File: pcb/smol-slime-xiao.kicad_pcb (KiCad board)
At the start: 4 copper layers, 20 x 23.5 mm, 12 parts, among them J1 Conn_01x02, J2 Conn_01x02, U1 ICM-45686, U3 1532H, U4 XIAO-nRF52840-SMD

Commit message: Add pours
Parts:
- moved C3 0.72 mm to (153.8, 108.3)
- moved R1 0.70 mm to (145.2, 107.3)
- moved R2 0.70 mm to (145.2, 109.0)
- moved U3 0.64 mm to (156.4, 92.5)
- moved R3 0.53 mm to (156.4, 89.4)
- moved J1 0.41 mm to (152.1, 101.0)
- moved U2 0.30 mm to (150.0, 108.8)
- moved J2 0.10 mm to (142.1, 92.5)
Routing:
- net GND: vias 0 -> 1
- net +5V: vias 0 -> 1
- added copper zone on B.Cu, net GND
- added copper zone on F.Cu, net GND
- added copper zone on In1.Cu, net GND
- added copper zone on In2.Cu, net VDD
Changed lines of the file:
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@@
 	(footprint "Resistor_SMD:R_0603_1608Metric"
 		(layer "F.Cu")
-		(at 156.75 89)
+		(at 156.4 89.4)
 		(descr "Resistor SMD 0603 (1608 Metric), square (rectangular) end terminal, IPC-7351 nominal, (Body size source: IPC-SM-782 page 72, https://www.pcb-3d.com/wordpress/wp-content/uploads/ipc-sm-782a_amendment_1_and_2.pdf), generated with kicad-footprint-generator")
 		(tags "resistor")
@@
 	(footprint "Generic:JST_PH2_SMT"
 		(layer "F.Cu")
-		(at 152.4575 101.05 90)
+		(at 152.05 101.05 90)
 		(descr "JST PH series connector, S2B-PH-K (http://www.jst-mfg.com/product/pdf/eng/ePH.pdf), generated with kicad-footprint-generator")
 		(tags "connector JST PH horizontal")
@@
 	(footprint "Resistor_SMD:R_0603_1608Metric"
 		(layer "F.Cu")
-		(at 145.25 109.75)
+		(at 145.25 109.05)
 		(descr "Resistor SMD 0603 (1608 Metric), square (rectangular) end terminal, IPC-7351 nominal, (Body size source: IPC-SM-782 page 72, https://www.pcb-3d.com/wordpress/wp-content/uploads/ipc-sm-782a_amendment_1_and_2.pdf), generated with kicad-footprint-generator")
 		(tags "resistor")
@@
 	(footprint "QMC6309:QMC6309"
 		(layer "F.Cu")
-		(at 150 109.05)
+		(at 150 108.75)
 		(property "Reference" "U2"
 			(at 1.75 0 0)
@@
 	(footprint "Crystal:Crystal_SMD_3225-4Pin_3.2x2.5mm"
 		(layer "F.Cu")
-		(at 156.9 92.1 180)
+		(at 156.4 92.5 180)
 		(descr "SMD3225/4, Crystal, 3.2x2.5mm package, SMD, generated with kicad-footprint-generator make_crystal.py, http://www.txccrystal.com/images/pdf/7m-accuracy.pdf")
 		(property "Reference" "U3"
@@
 	(footprint "Capacitor_SMD:C_0603_1608Metric"
 		(layer "F.Cu")
-		(at 153.75 109 90)
+		(at 153.75 108.275 90)
 		(descr "Capacitor SMD 0603 (1608 Metric), square (rectangular) end terminal, IPC-7351 nominal, (Body size source: IPC-SM-782 page 76, https://www.pcb-3d.com/wordpress/wp-content/uploads/ipc-sm-782a_amendment_1_and_2.pdf), generated with kicad-footprint-generator")
 		(tags "capacitor")
@@
 	(footprint "Resistor_SMD:R_0603_1608Metric"
 		(layer "F.Cu")
-		(at 145.25 108)
+		(at 145.25 107.3)
 		(descr "Resistor SMD 0603 (1608 Metric), square (rectangular) end terminal, IPC-7351 nominal, (Body size source: IPC-SM-782 page 72, https://www.pcb-3d.com/wordpress/wp-content/uploads/ipc-sm-782a_amendment_1_and_2.pdf), generated with kicad-footprint-generator")
 		(tags "resistor")
@@
 	(footprint "Generic:PinPads_1x02_P2.54mm"
 		(layer "F.Cu")
-		(at 142 92.5)
+		(at 142.1 92.5)
 		(descr "Through hole straight pin header, 1x02, 2.54mm pitch, single row")
 		(tags "Through hole pin header THT 1x02 2.54mm single row")
@@
 		)
 	)
+	(via
+		(at 142 95.04)
+		(size 0.5)
+		(drill 0.3)
+		(layers "F.Cu" "B.Cu")
+		(net 1)
+	)
+	(via
+		(at 142 92.5)
+		(size 0.5)
+		(drill 0.3)
+		(layers "F.Cu" "B.Cu")
+		(net 18)
+	)
+	(zone
+		(net 1)
+		(net_name "GND")
+		(layer "F.Cu")
+		(hatch edge 0.5)
+		(priority 1)
+		(connect_pads
+			(clearance 0.5)
+		)
+		(min_thickness 0.25)
+		(filled_areas_thickness no)
+		(fill yes
+			(thermal_gap 0.5)
+			(thermal_bridge_width 0.5)
+		)
+		(polygon
+			(pts
+				(xy 137.25 84.75) (xy 137.25 112.75) (xy 162.75 112.75) (xy 162.75 84.75)
+			)
+		)
+	)
+	(zone
+		(net 1)
+		(net_name "GND")
+		(layer "B.Cu")
+		(hatch edge 0.5)
+		(connect_pads
+			(clearance 0.5)
+		)
+		(min_thickness 0.25)
+		(filled_areas_thickness no)
+		(fill yes
+			(thermal_gap 0.5)
+			(thermal_bridge_width 0.5)
+		)
+		(polygon
+			(pts
+				(xy 137.5 85) (xy 137.5 112.5) (xy 162.5 112.5) (xy 162.5 85)
+			)
+		)
+	)
+	(zone
+		(net 1)
+		(net_name "GND")
+		(layer "In1.Cu")
+		(hatch edge 0.5)
+		(priority 2)
+		(connect_pads
+			(clearance 0.5)
+		)
+		(min_thickness 0.25)
+		(filled_areas_thickness no)
+		(fill yes
+			(thermal_gap 0.5)
+			(thermal_bridge_width 0.5)
+		)
+		(polygon
+			(pts
+				(xy 137 84.5) (xy 137 113) (xy 163 113) (xy 163 84.5)
+			)
+		)
+	)
+	(zone
+		(net 9)
+		(net_name "VDD")
+		(layer "In2.Cu")
+		(hatch edge 0.5)
+		(priority 3)
+		(connect_pads
+			(clearance 0.5)
+		)
+		(min_thickness 0.25)
+		(filled_areas_thickness no)
+		(fill yes
+			(thermal_gap 0.5)
+			(thermal_bridge_width 0.5)
+		)
+		(polygon
+			(pts
+				(xy 136.75 84.25) (xy 136.75 113.25) (xy 163.25 113.25) (xy 163.25 84.25)
+			)
+		)
+	)

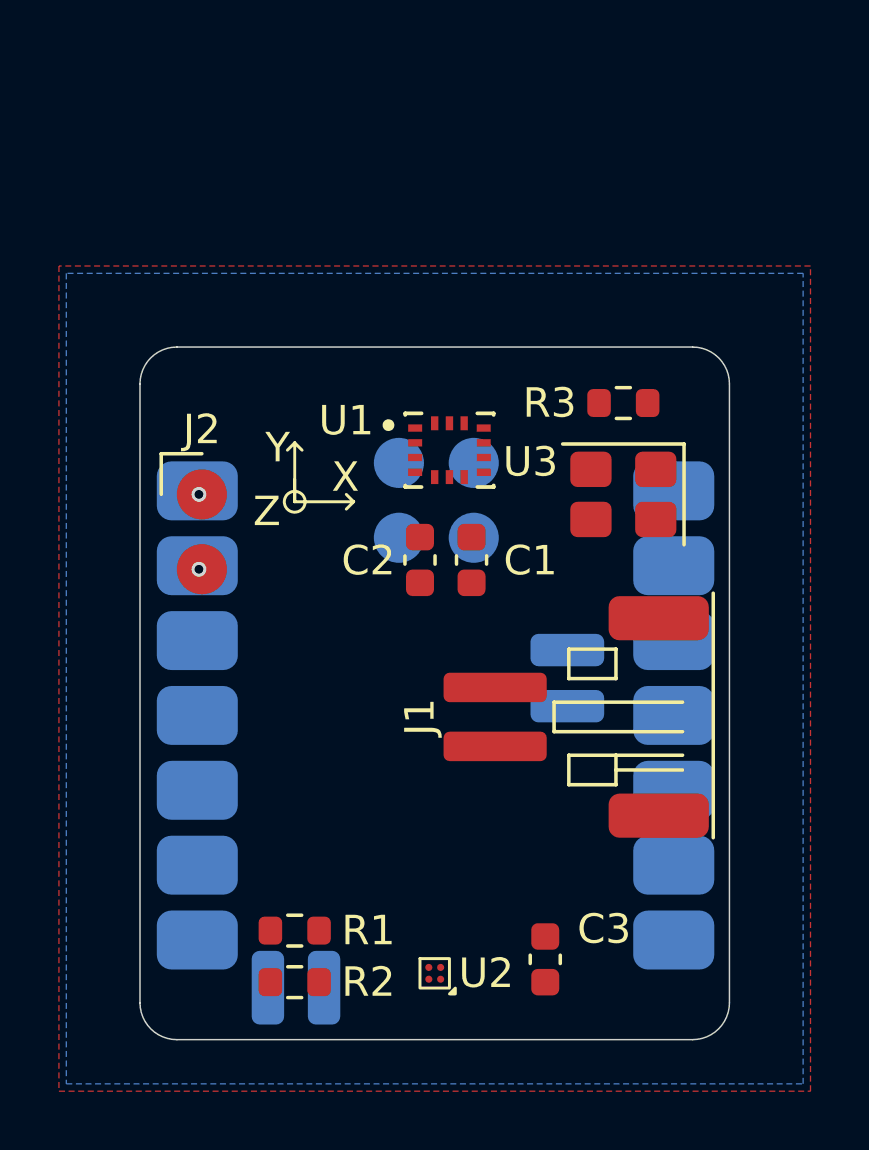
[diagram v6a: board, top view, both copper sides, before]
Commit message: Add descriptors
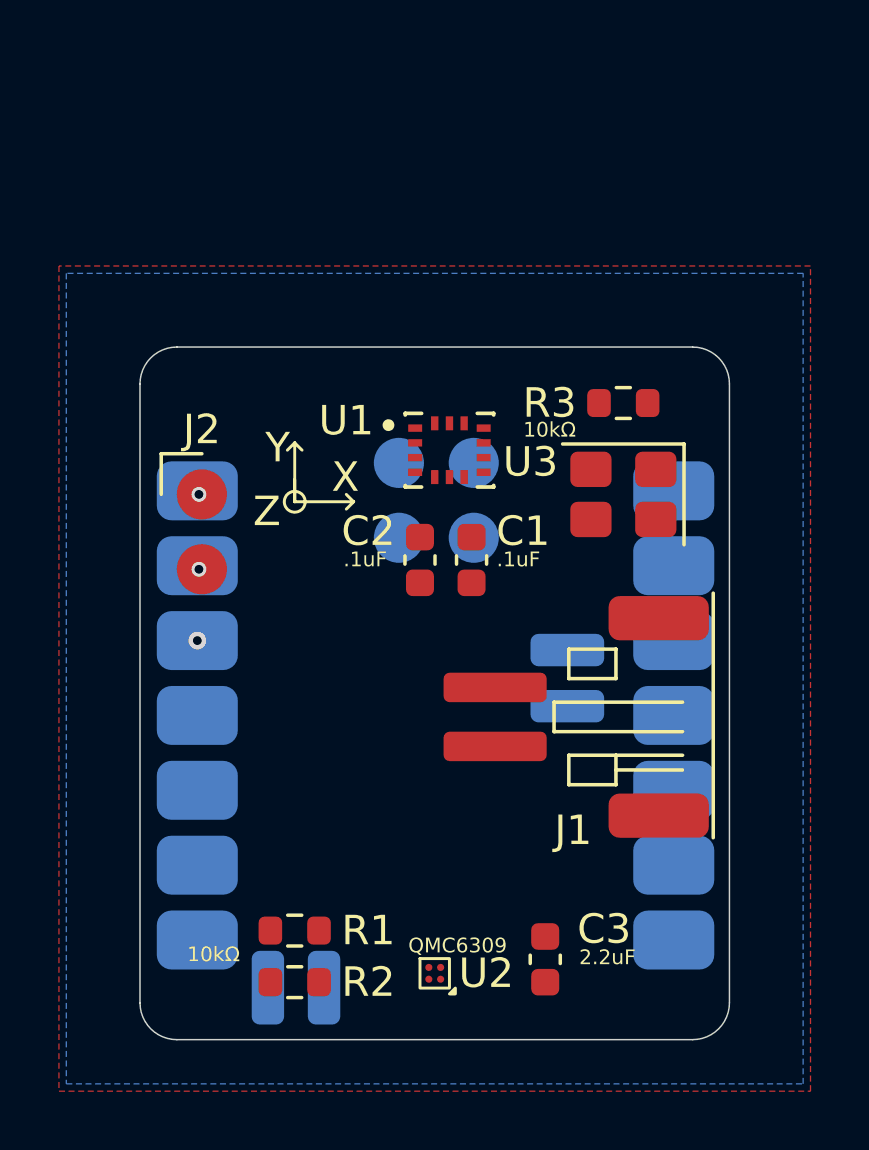
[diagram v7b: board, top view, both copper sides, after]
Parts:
- U2: value ~ -> (none)
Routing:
- net VDD: vias 0 -> 1
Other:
- board text added: ".1uF"
- board text added: "10kΩ"
- board text added: "2.2uF"
- board text added: "MEGNETOMETER KEEP OUT"
- board text added: "QMC6309"
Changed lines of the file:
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@@
 		(tags "connector JST PH horizontal")
 		(property "Reference" "J1"
-			(at 1 -2.55 90)
+			(at -2.85 2.65 180)
 			(layer "F.SilkS")
 			(effects
@@
 			)
 		)
-		(property "Value" "~"
+		(property "Value" ""
 			(at 0 1.25 0)
 			(unlocked yes)
@@
 		(tags "capacitor")
 		(property "Reference" "C1"
-			(at -0.025 2 180)
+			(at 0.975 1.75 180)
 			(layer "F.SilkS")
 			(effects
@@
 		(tags "capacitor")
 		(property "Reference" "C2"
-			(at -0.025 -1.75 180)
+			(at 0.975 -1.75 180)
 			(layer "F.SilkS")
 			(effects
@@
 		(layer "Edge.Cuts")
 	)
+	(gr_text ".1uF"
+		(at 146.9 95 0)
+		(layer "F.SilkS")
+		(effects
+			(font
+				(size 0.5 0.5)
+				(thickness 0.1)
+			)
+			(justify left bottom)
+		)
+	)
+	(gr_text ".1uF"
+		(at 152.1 95 0)
+		(layer "F.SilkS")
+		(effects
+			(font
+				(size 0.5 0.5)
+				(thickness 0.1)
+			)
+			(justify left bottom)
+		)
+	)
+	(gr_text "10kΩ"
+		(at 153 90.6 0)
+		(layer "F.SilkS")
+		(effects
+			(font
+				(size 0.5 0.5)
+				(thickness 0.1)
+			)
+			(justify left bottom)
+		)
+	)
+	(gr_text "2.2uF"
+		(at 154.9 108.5 0)
+		(layer "F.SilkS")
+		(effects
+			(font
+				(size 0.5 0.5)
+				(thickness 0.1)
+			)
+			(justify left bottom)
+		)
+	)
 	(gr_text "X"
 		(at 146.5 92.5 0)
@@
 		)
 	)
+	(gr_text "10kΩ"
+		(at 141.6 108.4 0)
+		(layer "F.SilkS")
+		(effects
+			(font
+				(size 0.5 0.5)
+				(thickness 0.1)
+			)
+			(justify left bottom)
+		)
+	)
 	(gr_text "Z"
 		(at 143.835787 93.664214 0)
@@
 		)
 	)
+	(gr_text "QMC6309"
+		(at 149.1 108.1 0)
+		(layer "F.SilkS")
+		(effects
+			(font
+				(size 0.5 0.5)
+				(thickness 0.1)
+			)
+			(justify left bottom)
+		)
+	)
 	(gr_text "Y"
 		(at 144.25 91.5 0)
@@
 		)
 	)
+	(gr_text "MEGNETOMETER KEEP OUT"
+		(at 140 112.25 0)
+		(layer "Cmts.User")
+		(effects
+			(font
+				(size 1 1)
+				(thickness 0.15)
+			)
+			(justify left bottom)
+		)
+	)
 	(via
 		(at 142 95.04)
@@
 		(layers "F.Cu" "B.Cu")
 		(net 1)
+	)
+	(via
+		(at 141.945 97.46)
+		(size 0.6)
+		(drill 0.3)
+		(layers "F.Cu" "B.Cu")
+		(net 9)
 	)
 	(via
@@
 			)
 		)
+	)
+	(zone
+		(net 0)
+		(net_name "")
+		(layers "F.Cu" "B.Cu" "In1.Cu" "In2.Cu")
+		(hatch edge 0.5)
+		(connect_pads
+			(clearance 0)
+		)
+		(min_thickness 0.25)
+		(filled_areas_thickness no)
+		(keepout
+			(tracks allowed)
+			(vias allowed)
+			(pads allowed)
+			(copperpour not_allowed)
+			(footprints allowed)
+		)
+		(placement
+			(enabled no)
+			(sheetname "/")
+		)
+		(fill
+			(thermal_gap 0.5)
+			(thermal_bridge_width 0.5)
+		)
+		(polygon
+			(pts
+				(xy 160 111) (xy 140 111) (xy 140 106.25) (xy 160 106.25)
+			)
+		)

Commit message: Move CLK_CTL to alternate GPIO
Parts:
- U2: value (none) -> ~
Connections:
- U4 pad 2: unconnected-(U4-P0.03_A1_D1-Pad2) -> /CLK_CTL
- U4 pad 7: /CLK_CTL -> unconnected-(U4-P1.11_D6_TX-Pad7)
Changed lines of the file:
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@@
 	(net 24 "unconnected-(U4-PA31_SWDIO-Pad19)")
 	(net 25 "unconnected-(U4-PA30_SWCLK-Pad20)")
-	(net 26 "unconnected-(U4-P0.03_A1_D1-Pad2)")
+	(net 26 "unconnected-(U4-P1.11_D6_TX-Pad7)")
 	(net 27 "unconnected-(U4-P0.02_A0_D0-Pad1)")
 	(net 28 "unconnected-(J1-Pin_3-Pad3)")
@@
 			)
 		)
-		(property "Value" ""
+		(property "Value" "~"
 			(at 0 1.25 0)
 			(unlocked yes)
@@
 			(layers "B.Cu" "B.Mask" "B.Paste")
 			(roundrect_rratio 0.25)
-			(net 26 "unconnected-(U4-P0.03_A1_D1-Pad2)")
+			(net 8 "/CLK_CTL")
 			(pinfunction "P0.03_A1_D1")
-			(pintype "passive+no_connect")
+			(pintype "passive")
 			(solder_mask_margin 0.0508)
 			(thermal_bridge_angle 45)
@@
 			(layers "B.Cu" "B.Mask" "B.Paste")
 			(roundrect_rratio 0.25)
-			(net 8 "/CLK_CTL")
+			(net 26 "unconnected-(U4-P1.11_D6_TX-Pad7)")
 			(pinfunction "P1.11_D6_TX")
-			(pintype "passive")
+			(pintype "passive+no_connect")
 			(solder_mask_margin 0.0508)
 			(thermal_bridge_angle 45)
